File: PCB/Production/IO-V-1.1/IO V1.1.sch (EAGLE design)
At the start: 71 parts, among them IC10 74273N, IC11 74LS10N, IC2 MAX232, IC3 74LS244N, IC4 74273N, IC5 74LS138N, IC6 74LS10N, IC7 74LS00N, IC8 74LS06N, IC9 74273N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

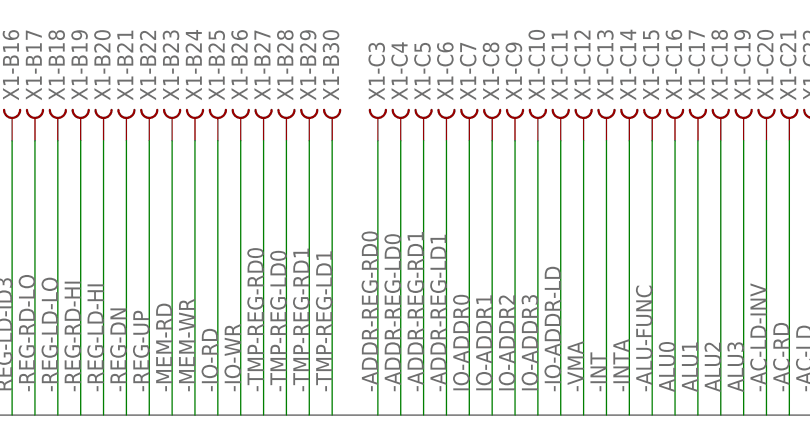
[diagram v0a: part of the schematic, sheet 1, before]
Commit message: Cleanup Bus signals
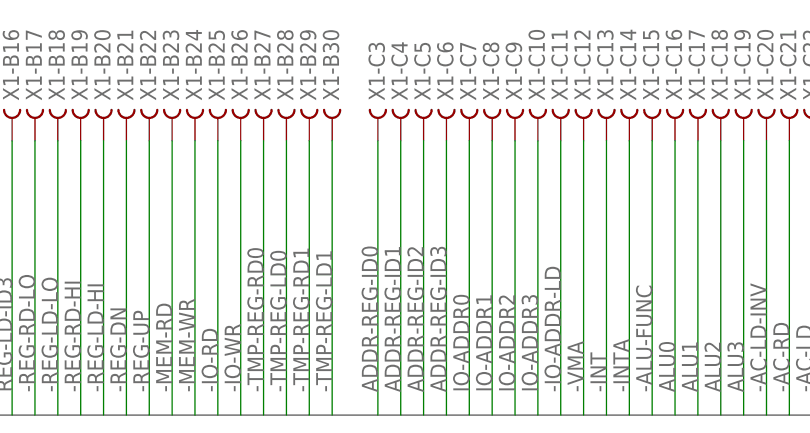
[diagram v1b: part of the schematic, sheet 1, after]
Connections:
- net -ADDR-REG-LD0 renamed ADDR-REG-ID1
- net -ADDR-REG-LD1 renamed ADDR-REG-ID3
- net -ADDR-REG-RD0 renamed ADDR-REG-ID0
- net -ADDR-REG-RD1 renamed ADDR-REG-ID2
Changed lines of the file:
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@@
 </instances>
 <busses>
-<bus name="-AC-LD,-AC-LD-INV,-AC-RD,ADDR[0..15],-ADDR-REG-LD[0..1],-ADDR-REG-RD[0..1],ALU[0..3],-ALU-FUNC,BR-COND,-BUS-EN,DATA[0..15],-HL-SWAP,IN,-INT,-INTA,IO-ADDR[0..3],-IO-ADDR-LD,-IO-RD,-IO-WR,-MEM-RD,-MEM-WR,OUT,-REG-DN,-REG-FUNC-LD,-REG-FUNC-RD,-REG-LD-HI,REG-LD-ID[0..3],-REG-LD-LO,-REG-RD-HI,REG-RD-ID[0..3],-REG-RD-LO,-REG-UP,-RESET,-RUN,-SR-LD,-TMP-REG-LD[0..1],-TMP-REG-RD[0..1],-VMA">
+<bus name="-AC-LD,-AC-LD-INV,-AC-RD,ADDR[0..15],ADDR-REG-ID0,ADDR-REG-ID1,ADDR-REG-ID2,ADDR-REG-ID3,ALU[0..3],-ALU-FUNC,BR-COND,-BUS-EN,DATA[0..15],-HL-SWAP,IN,-INT,-INTA,IO-ADDR[0..3],-IO-ADDR-LD,-IO-RD,-IO-WR,-MEM-RD,-MEM-WR,OUT,-REG-DN,-REG-FUNC-LD,-REG-FUNC-RD,-REG-LD-HI,REG-LD-ID[0..3],-REG-LD-LO,-REG-RD-HI,REG-RD-ID[0..3],-REG-RD-LO,-REG-UP,-RESET,-RUN,-SR-LD,-TMP-REG-LD[0..1],-TMP-REG-RD[0..1],-VMA">
 <segment>
 <wire x1="-33.02" y1="-1.27" x2="182.88" y2="-1.27" width="0.762" layer="92"/>
@@
 </segment>
 </net>
-<net name="-ADDR-REG-RD0" class="0">
+<net name="ADDR-REG-ID0" class="0">
 <segment>
 <pinref part="X1" gate="-C3" pin="B"/>
@@
 </segment>
 </net>
-<net name="-ADDR-REG-LD0" class="0">
+<net name="ADDR-REG-ID1" class="0">
 <segment>
 <pinref part="X1" gate="-C4" pin="B"/>
@@
 </segment>
 </net>
-<net name="-ADDR-REG-RD1" class="0">
+<net name="ADDR-REG-ID2" class="0">
 <segment>
 <pinref part="X1" gate="-C5" pin="B"/>
@@
 </segment>
 </net>
-<net name="-ADDR-REG-LD1" class="0">
+<net name="ADDR-REG-ID3" class="0">
 <segment>
 <pinref part="X1" gate="-C6" pin="B"/>
